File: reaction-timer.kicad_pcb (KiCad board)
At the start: 2 copper layers, 48 x 80 mm, 38 parts, among them IC1 4026, IC2 4026, IC3 4026, IC5 NE555P, IC6 NE555P, IC7 NE555P

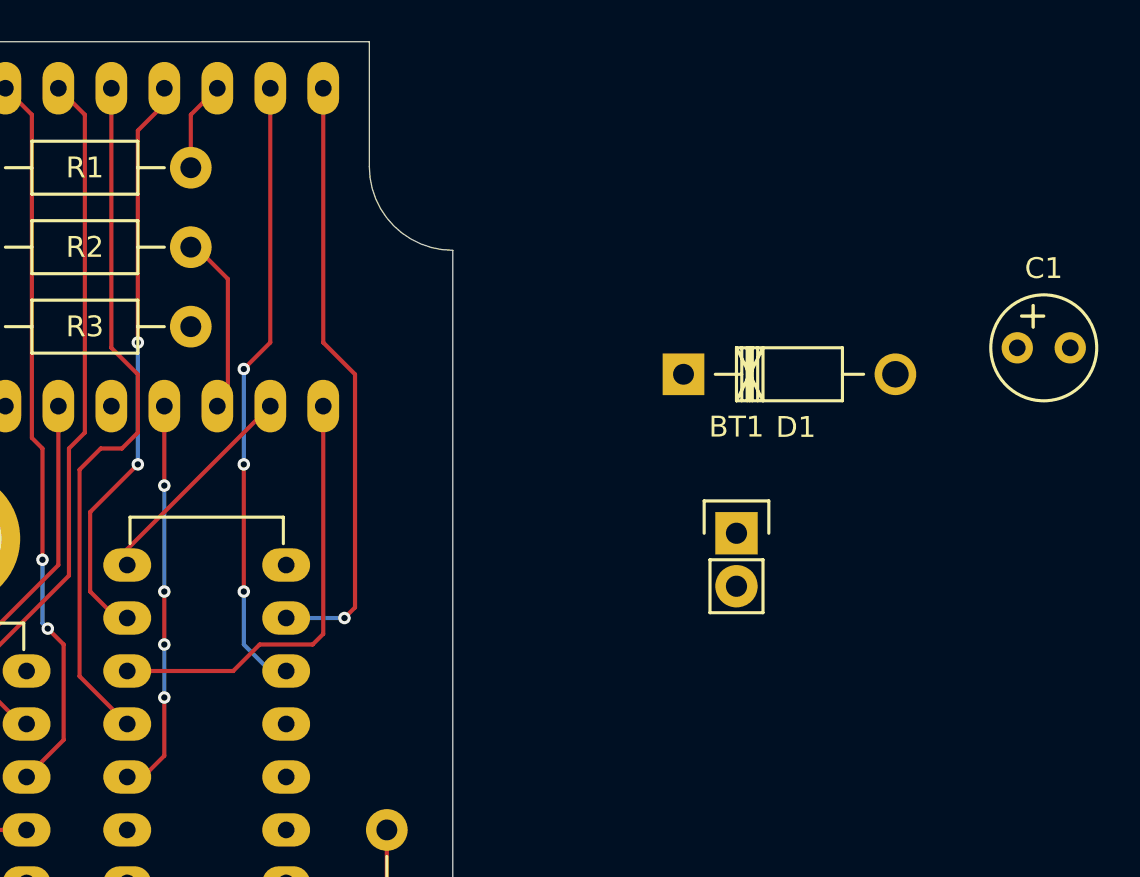
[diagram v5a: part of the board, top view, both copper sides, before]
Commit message: Move IC1 wiring
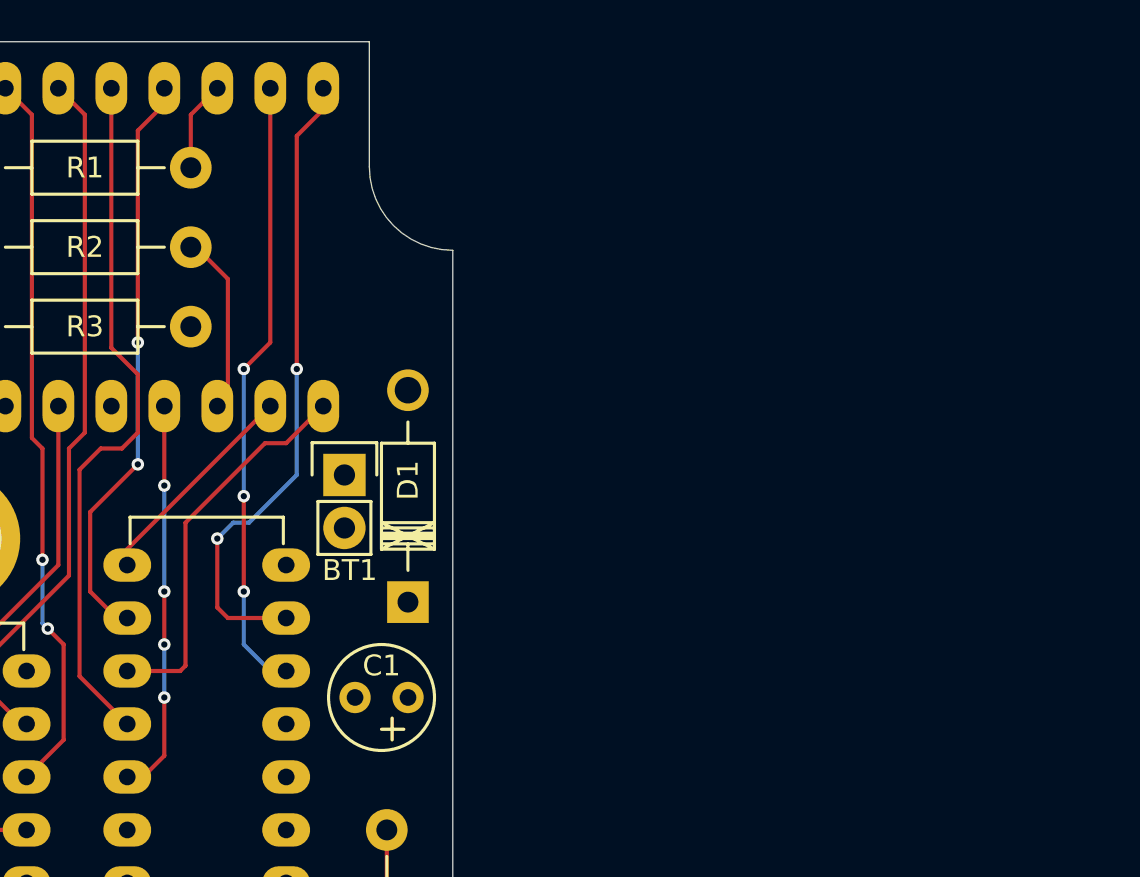
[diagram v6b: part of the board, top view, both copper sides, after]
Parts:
- moved C1 33.7 mm to (103.1, 92.7), turned to 180 degrees
- moved BT1 19.0 mm to (100.1, 82.0)
- moved D1 17.1 mm to (103.1, 88.1), turned to 90 degrees
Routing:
- net /E1: track 21.1 -> 18.7 mm
- net /G1: track 29.0 -> 31.0 mm, vias 1 -> 2

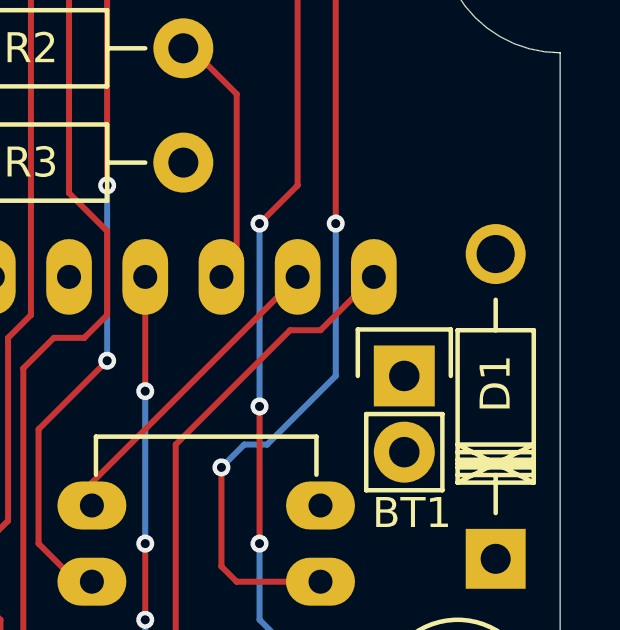
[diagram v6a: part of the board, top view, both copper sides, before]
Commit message: Add +9V to the Power net class
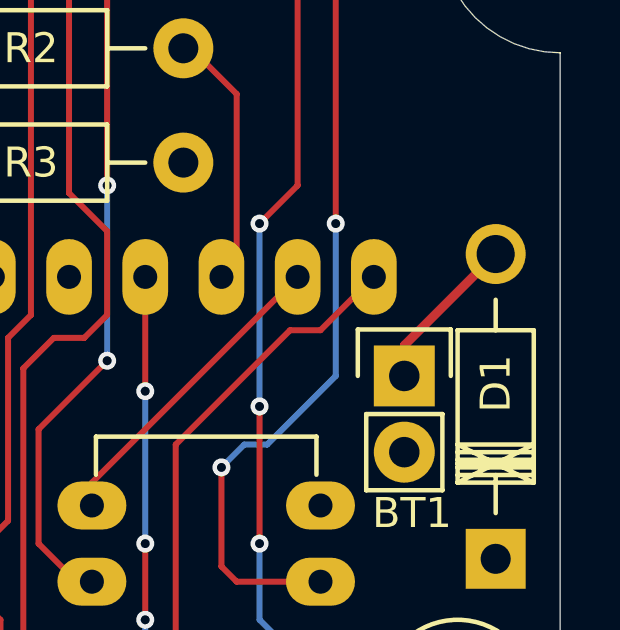
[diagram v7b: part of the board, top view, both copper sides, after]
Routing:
- net +9V: track 0.00 -> 5.33 mm
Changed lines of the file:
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@@
   (general
     (links 104)
-    (no_connects 51)
+    (no_connects 50)
     (area 57.269499 61.269499 105.270501 141.270501)
     (thickness 1.6)
     (drawings 8)
-    (tracks 262)
+    (tracks 264)
     (zones 0)
     (modules 38)
@@
     (uvia_drill 0.1)
     (uvias_allowed no)
-    (uvia_min_size 0.2)
-    (uvia_min_drill 0.1)
+    (uvia_min_size 0)
+    (uvia_min_drill 0)
     (pcb_text_width 0.3)
     (pcb_text_size 1.5 1.5)
@@
     (uvia_dia 0.3)
     (uvia_drill 0.1)
-    (add_net +9V)
     (add_net /A1)
     (add_net /A2)
@@
     (uvia_dia 0.3)
     (uvia_drill 0.1)
+    (add_net +9V)
   )
   (module Displays_7-Segment:7SegmentLED_LTS6760_LTS6780 (layer B.Cu)
@@
   (segment (start 73.66 88.9) (end 74.676 87.884) (width 0.2) (layer F.Cu) (net 30))
   (segment (start 72.39 88.9) (end 73.66 88.9) (width 0.2) (layer F.Cu) (net 30))
+  (segment (start 100.076 82.042) (end 100.076 81.02346) (width 0.3) (layer F.Cu) (net 31) (status 400000))
+  (segment (start 100.076 81.02346) (end 103.12146 77.978) (width 0.3) (layer F.Cu) (net 31) (status 800000))
   (segment (start 97.282 111.252) (end 97.536 111.252) (width 0.2) (layer F.Cu) (net 33))
   (segment (start 97.536 111.252) (end 102.108 106.68) (width 0.2) (layer F.Cu) (net 33))

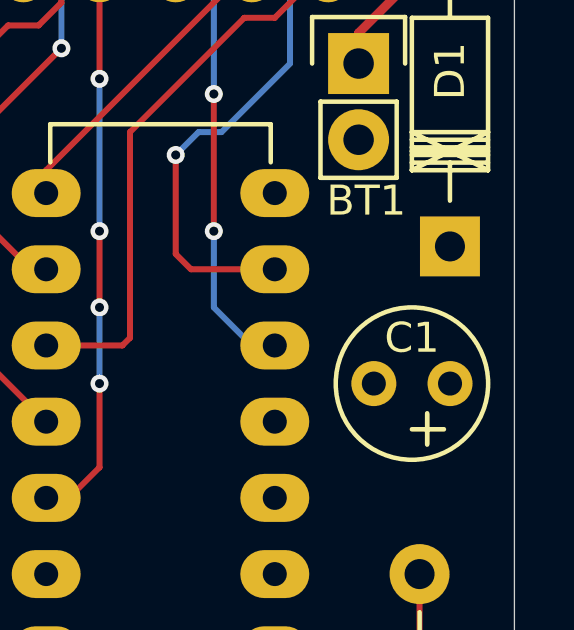
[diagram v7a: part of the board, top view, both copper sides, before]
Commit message: Connect +9V to filter cap C1
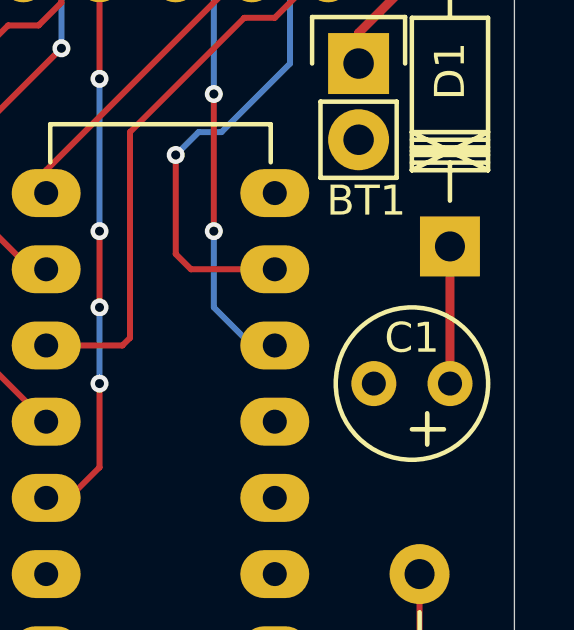
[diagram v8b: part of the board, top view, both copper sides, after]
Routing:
- net Net-(C1-Pad1): track 14.3 -> 18.9 mm
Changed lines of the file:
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@@
   (general
     (links 104)
-    (no_connects 50)
+    (no_connects 49)
     (area 57.269499 61.269499 105.270501 141.270501)
     (thickness 1.6)
     (drawings 8)
-    (tracks 264)
+    (tracks 266)
     (zones 0)
     (modules 38)
@@
     (add_net "Net-(AFF3-Pad5)")
     (add_net "Net-(AFF3-Pad8)")
-    (add_net "Net-(C1-Pad1)")
     (add_net "Net-(C2-Pad1)")
     (add_net "Net-(C3-Pad1)")
@@
     (uvia_drill 0.1)
     (add_net +9V)
+    (add_net "Net-(C1-Pad1)")
   )
   (module Displays_7-Segment:7SegmentLED_LTS6760_LTS6780 (layer B.Cu)
@@
   (segment (start 73.66 88.9) (end 74.676 87.884) (width 0.2) (layer F.Cu) (net 30))
   (segment (start 72.39 88.9) (end 73.66 88.9) (width 0.2) (layer F.Cu) (net 30))
-  (segment (start 100.076 82.042) (end 100.076 81.02346) (width 0.3) (layer F.Cu) (net 31) (status 400000))
-  (segment (start 100.076 81.02346) (end 103.12146 77.978) (width 0.3) (layer F.Cu) (net 31) (status 800000))
+  (segment (start 100.076 82.042) (end 100.076 81.02346) (width 0.3) (layer F.Cu) (net 31))
+  (segment (start 100.076 81.02346) (end 103.12146 77.978) (width 0.3) (layer F.Cu) (net 31))
+  (segment (start 103.12146 88.138) (end 103.12146 92.70746) (width 0.3) (layer F.Cu) (net 33) (status C00000))
+  (segment (start 103.12146 92.70746) (end 103.124 92.71) (width 0.3) (layer F.Cu) (net 33) (status C00000))
   (segment (start 97.282 111.252) (end 97.536 111.252) (width 0.2) (layer F.Cu) (net 33))
   (segment (start 97.536 111.252) (end 102.108 106.68) (width 0.2) (layer F.Cu) (net 33))
